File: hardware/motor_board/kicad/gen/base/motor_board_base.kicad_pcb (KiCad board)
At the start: 4 copper layers, 75 x 35 mm, 237 parts, among them J1 BOOMELE_1.27-2x10P, J2 WAFER-SH1.0-6PWB, J3 WAFER-SH1.0-6PWB, J4 S5B-XH-A, Q1 HYG015N04LS1C2, Q2 HYG015N04LS1C2, Q3 HYG015N04LS1C2, Q4 HYG015N04LS1C2, Q5 HYG015N04LS1C2, Q6 HYG015N04LS1C2, Q7 HYG015N04LS1C2, Q8 HYG015N04LS1C2, U1 STM32G474RET6, U10 SN74LVC3G17DCUR, U11 TPS22945DCKR, U12 TPS22945DCKR, U13 LM74502DDFR, U14 74LVC1G17SE-7, U2 DRV8323RHRGZR, U3 DRV8316CRRGFR, U4 DRV8316CRRGFR, U5 AP2112K-3.3TRG1, U6 SN74LVC08APWR, U7 INA239AIDGSR, U8 BQ76907RGRR, U9 SN74LVC3G17DCUR

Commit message: motor_board routing block 6b: motor outputs (0.8 mm top lanes, pin order = connector order), U3/U4 GND pins 15/18 into the EP; TP2/TP4 over U1's front row
Co-Authored-By: Claude Opus 5.5 (1M context) <noreply@anthropic.com>
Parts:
- moved TP4 20.4 mm to (135.6, 90.2)
- moved TP2 20.2 mm to (133.4, 90.2)
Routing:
- net GND: track 91.5 -> 87.3 mm, vias 173 -> 169
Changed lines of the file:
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@@
 	(footprint "TestPoint:TestPoint_Pad_D1.0mm"
 		(layer "F.Cu")
-		(at 117.2 99.25)
+		(at 135.55 90.25)
 		(descr "SMD pad as test Point, diameter 1.0mm")
 		(tags "test point SMD pad")
@@
 	(footprint "TestPoint:TestPoint_Pad_D1.0mm"
 		(layer "F.Cu")
-		(at 115 98.7)
+		(at 133.4 90.25)
 		(descr "SMD pad as test Point, diameter 1.0mm")
 		(tags "test point SMD pad")
@@
 	)
 	(segment
-		(start 169.9 93.75)
-		(end 170.945 93.75)
-		(width 0.25)
-		(layer "F.Cu")
-		(net "GND")
-	)
-	(segment
 		(start 161.5 98.68)
 		(end 161.15 100.105)
@@
 	)
 	(segment
-		(start 119.6 99.25)
-		(end 118.555 99.25)
-		(width 0.25)
-		(layer "F.Cu")
-		(net "GND")
-	)
-	(segment
 		(start 128.65 97.63)
 		(end 127.195 97.979999)
@@
 	)
 	(segment
-		(start 119.6 100.75)
-		(end 118.555 100.75)
-		(width 0.25)
-		(layer "F.Cu")
-		(net "GND")
-	)
-	(segment
 		(start 158 99.95)
 		(end 158.35 100.795)
@@
 	)
 	(segment
-		(start 169.9 95.25)
-		(end 170.945 95.25)
-		(width 0.25)
-		(layer "F.Cu")
-		(net "GND")
-	)
-	(segment
 		(start 150.0625 95.25)
 		(end 151.125 95.25)
@@
 	)
 	(via
-		(at 118.555 100.75)
-		(size 0.45)
-		(drill 0.25)
-		(layers "F.Cu" "B.Cu")
-		(net "GND")
-	)
-	(via
 		(at 135.31 77.184999)
 		(size 0.45)
@@
 	)
 	(via
-		(at 170.945 93.75)
-		(size 0.45)
-		(drill 0.25)
-		(layers "F.Cu" "B.Cu")
-		(net "GND")
-	)
-	(via
 		(at 153.799999 83.9)
 		(size 0.6)
@@
 	)
 	(via
-		(at 170.945 95.25)
-		(size 0.45)
-		(drill 0.25)
-		(layers "F.Cu" "B.Cu")
-		(net "GND")
-	)
-	(via
 		(at 142.9 85.899999)
 		(size 0.6)
@@
 		(size 0.45)
 		(drill 0.25)
-		(layers "F.Cu" "B.Cu")
-		(net "GND")
-	)
-	(via
-		(at 118.555 99.25)
-		(size 0.45)
-		(drill 0.25)

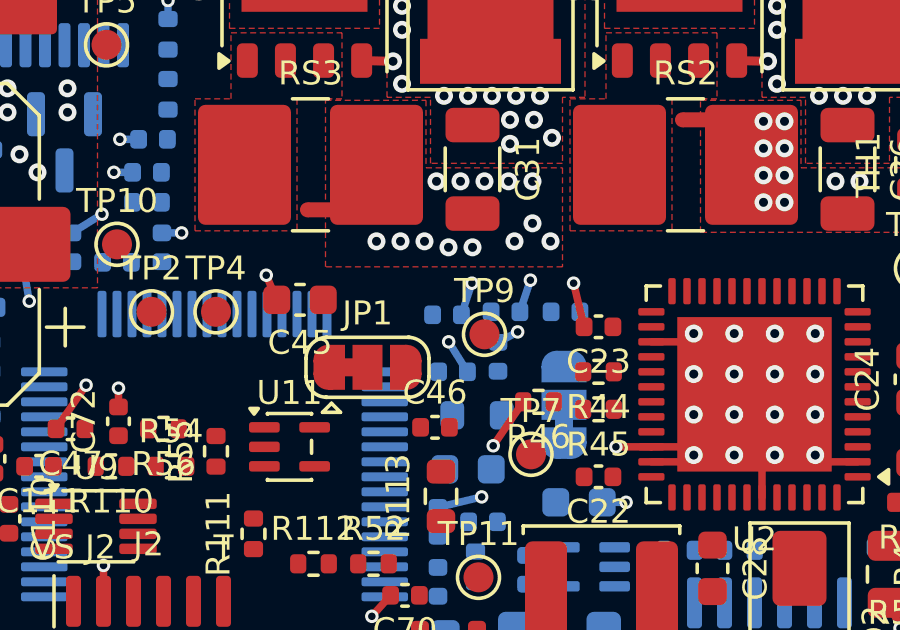
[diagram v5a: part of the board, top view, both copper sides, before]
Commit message: motor_board routing block 7b: U2 current-sense outputs (W_SOA/B/C) untangled from phase C's escape and routed to U1
SNC Kelvin lane moved to y 17.9 (stair via tucked into the VBAT feed edge), SHC stair via 0.1 west,
VREF hand-drawn, C23 0.35 mm rearward, three stitching/pad GND vias dropped (re-placed at close-out).
Tools: geo_why.py / geo_near.py (what blocks a spot, nearest legal spots), net_ends.py.

Co-Authored-By: Claude Opus 5.5 (1M context) <noreply@anthropic.com>
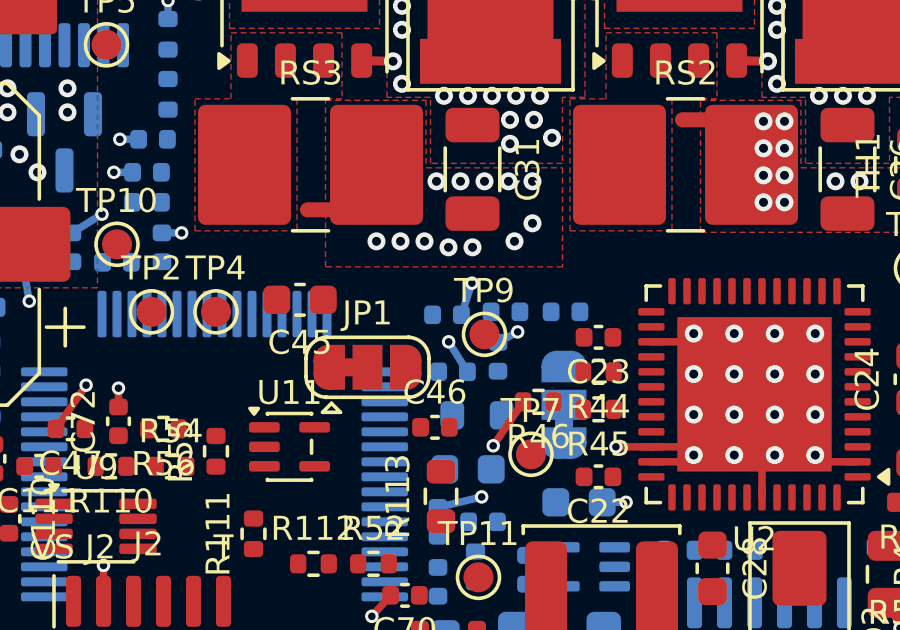
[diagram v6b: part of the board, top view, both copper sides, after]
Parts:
- moved C23 0.35 mm to (148.3, 91.1)
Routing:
- net GND: track 87.3 -> 83.8 mm, vias 169 -> 165
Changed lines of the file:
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@@
 	(footprint "Capacitor_SMD:C_0402_1005Metric"
 		(layer "F.Cu")
-		(at 148.3 90.75 180)
+		(at 148.3 91.1 180)
 		(descr "Capacitor SMD 0402 (1005 Metric), square (rectangular) end terminal, IPC-7351 nominal, (Body size source: IPC-SM-782 page 76, https://www.pcb-3d.com/wordpress/wp-content/uploads/ipc-sm-782a_amendment_1_and_2.pdf)")
 		(tags "capacitor")
@@
 	)
 	(segment
-		(start 137.575 89.85)
-		(end 137.225 89.03)
-		(width 0.25)
-		(layer "F.Cu")
-		(net "GND")
-	)
-	(segment
 		(start 125.25 97.6)
 		(end 125.25 98.35)
@@
 	)
 	(segment
-		(start 147.82 90.75)
-		(end 147.47 89.295)
-		(width 0.25)
-		(layer "F.Cu")
-		(net "GND")
-	)
-	(segment
 		(start 130.219999 94.15)
 		(end 131.219999 92.695)
@@
 	)
 	(via
-		(at 147.47 89.295)
-		(size 0.45)
-		(drill 0.25)
-		(layers "F.Cu" "B.Cu")
-		(net "GND")
-	)
-	(via
-		(at 146.7 87.899999)
-		(size 0.6)
-		(drill 0.3)
-		(layers "F.Cu" "B.Cu")
-		(net "GND")
-	)
-	(via
 		(at 143.3 88.099999)
 		(size 0.6)
@@
 	)
 	(via
-		(at 137.225 89.03)
-		(size 0.45)
-		(drill 0.25)
-		(layers "F.Cu" "B.Cu")
-		(net "GND")
-	)
-	(via
 		(at 161.85 93.145)
 		(size 0.45)
@@
 	)
 	(via
-		(at 146.03 89.195)
-		(size 0.45)
-		(drill 0.25)
-		(layers "F.Cu" "B.Cu")
-		(net "GND")
-	)
-	(via
 		(at 102.3 83.055)
 		(size 0.45)
@@
 		(width 0.25)
 		(layer "B.Cu")
-		(net "GND")
-	)
-	(segment
-		(start 145.68 90.25)
-		(end 146.03 89.195)
-		(width 0.25)
-		(layer "B.Cu")

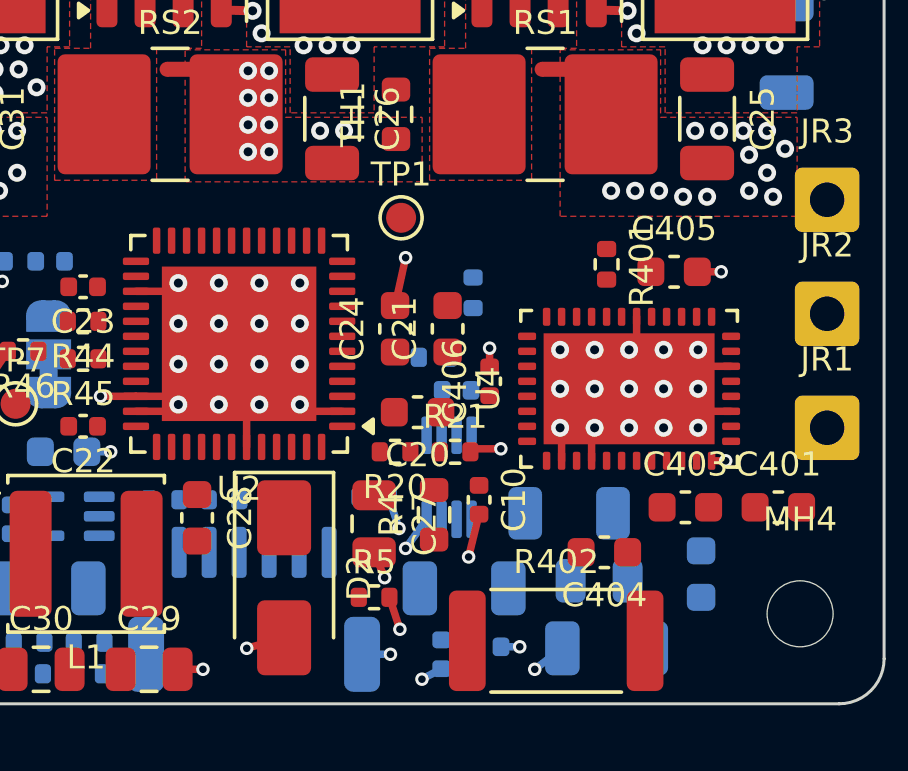
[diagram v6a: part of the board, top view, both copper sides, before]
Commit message: motor_board routing blocks 7c/7d: U4 escape (front row, left side; C405/R401 re-placed, C406 to the bottom) and U2 rear escape (C28 moved back, bootstrap re-drawn)
Co-Authored-By: Claude Opus 5.5 (1M context) <noreply@anthropic.com>
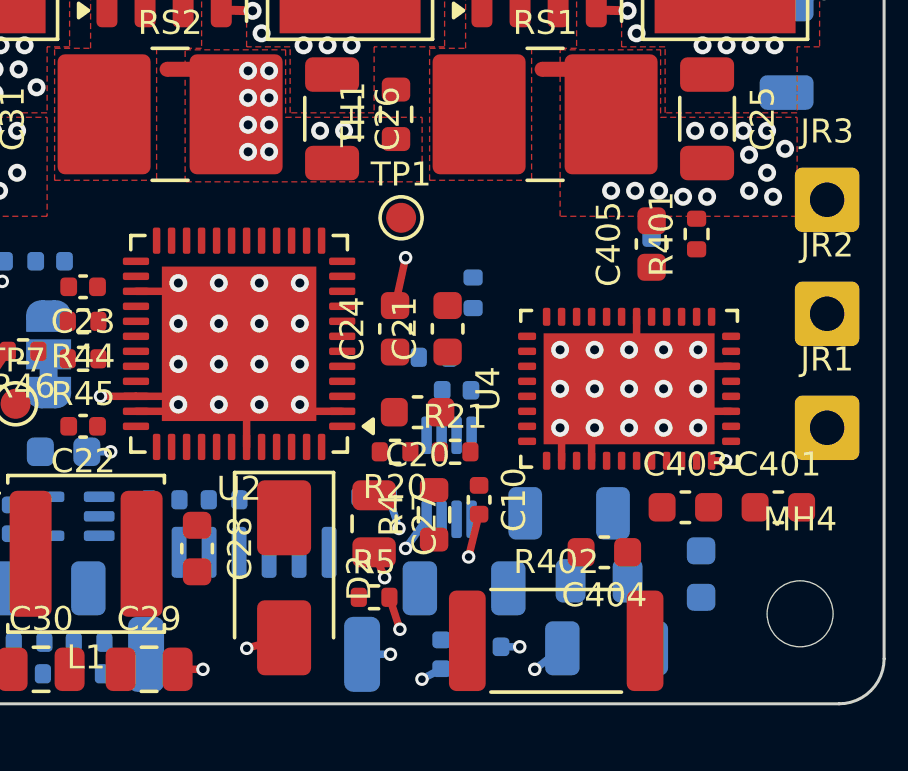
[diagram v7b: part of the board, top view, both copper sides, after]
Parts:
- C406: moved to B.Cu
- moved C406 6.89 mm to (167.2, 90.0)
- moved R401 3.17 mm to (168.8, 89.3), turned to 90 degrees
- moved C405 1.19 mm to (167.2, 89.7), turned to 90 degrees
- moved C28 1.03 mm to (152.1, 99.8)
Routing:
- net GND: track 83.8 -> 81.4 mm, vias 165 -> 162

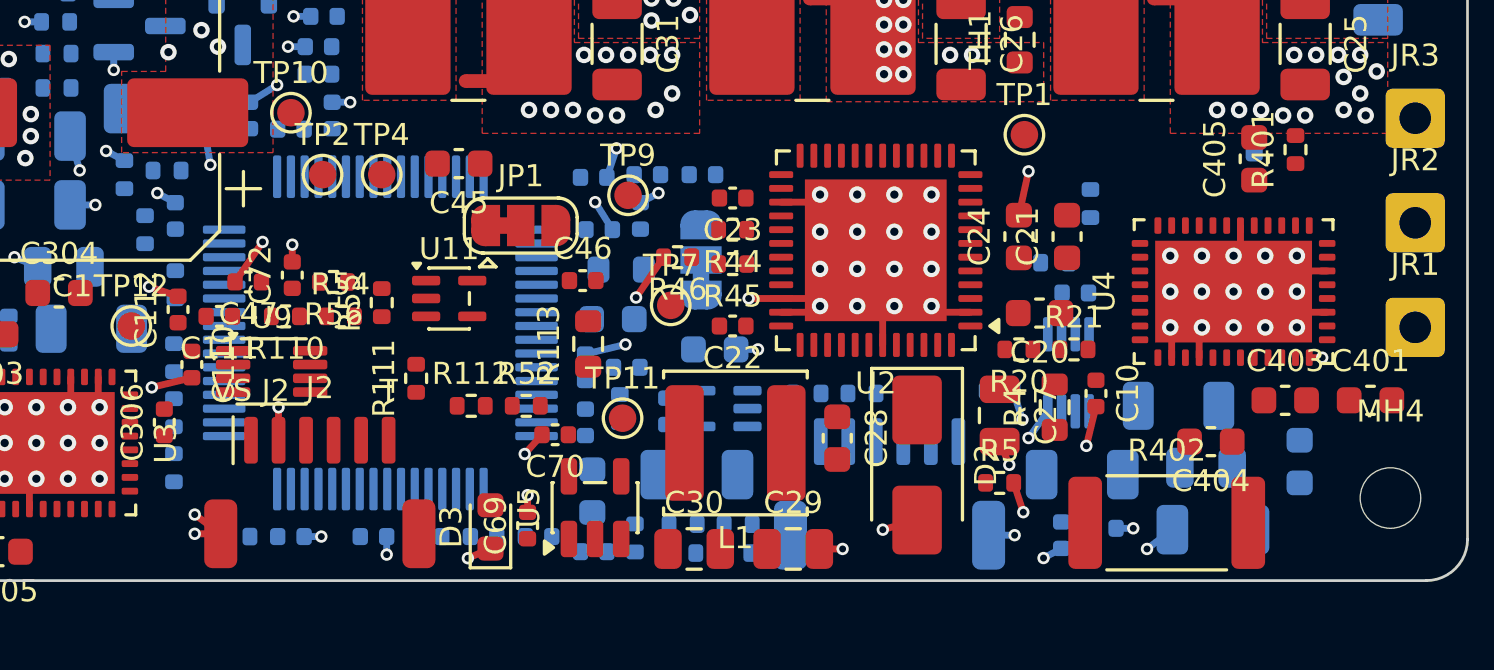
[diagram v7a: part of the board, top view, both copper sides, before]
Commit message: motor_board routing block 8: east bus (L3) complete U1<->U4
Twelve planned L3 lanes behind U2; U4 front group round U1's NE corner into its
top-row vias, INHA/INHC through the right-column gap, south group round U1's rear.
CSA filters R80/R81 moved to the top at U4's corner and R82 beside U1.25
(they sat west of U1, the wrong side for both ends); C90/C91 swapped so the
outer lanes drop straight into them. nCS hops once on top between J2's pins.
Router gains a per-request tol. DRC 0, 285 unconnected.

Co-Authored-By: Claude Opus 5.5 (1M context) <noreply@anthropic.com>
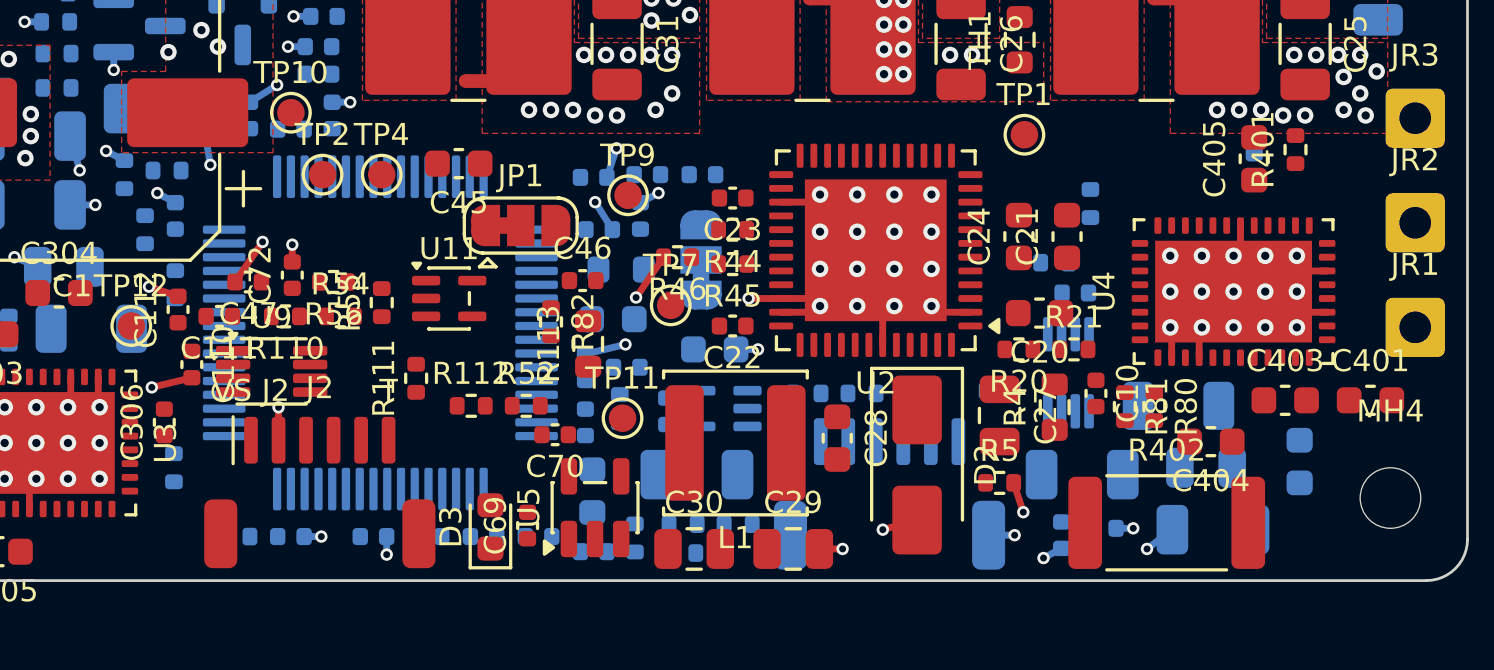
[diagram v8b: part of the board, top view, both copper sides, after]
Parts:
- R80, R81, R82: moved to F.Cu
- moved R80 35.6 mm to (163.6, 98.7)
- moved R81 34.6 mm to (162.6, 98.7)
- moved R82 10.8 mm to (141.7, 95.6), turned to -90 degrees
- moved C90 2.00 mm to (141.2, 103.4)
- moved C91 2.00 mm to (139.2, 103.4)
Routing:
- net GND: track 81.4 -> 70.0 mm, vias 162 -> 151
